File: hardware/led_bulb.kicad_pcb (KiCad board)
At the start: 2 copper layers, 92.4 x 91.4 mm, 170 parts, among them P1 USB_OTG, P10 CONN_01X02, P11 CONN_01X02, P12 CONN_01X02, P13 CONN_01X02, P14 CONN_01X02, P15 CONN_01X02, P16 CONN_01X02, P17 CONN_01X02, P18 CONN_01X02, P19 CONN_01X02, P2 CONN_01X02, P20 CONN_01X02, P21 CONN_01X02, P22 CONN_01X02, P23 CONN_01X02, P24 CONN_01X02, P25 CONN_01X02, P26 CONN_01X02, P27 CONN_01X02, P28 CONN_01X02, P29 CONN_01X02, P3 CONN_01X02, P30 CONN_01X02, P31 CONN_01X02, P32 CONN_01X02, P33 CONN_01X02, P4 CONN_01X02, P5 CONN_01X02, P6 CONN_01X02, P7 CONN_01X02, P8 CONN_01X02, P9 CONN_01X02, Q1 S8050, Q2 S8050, SW1 RST, SW2 FLASH, U1 CP2102-GM, U3 ESP-12E, U4 AP1117D33

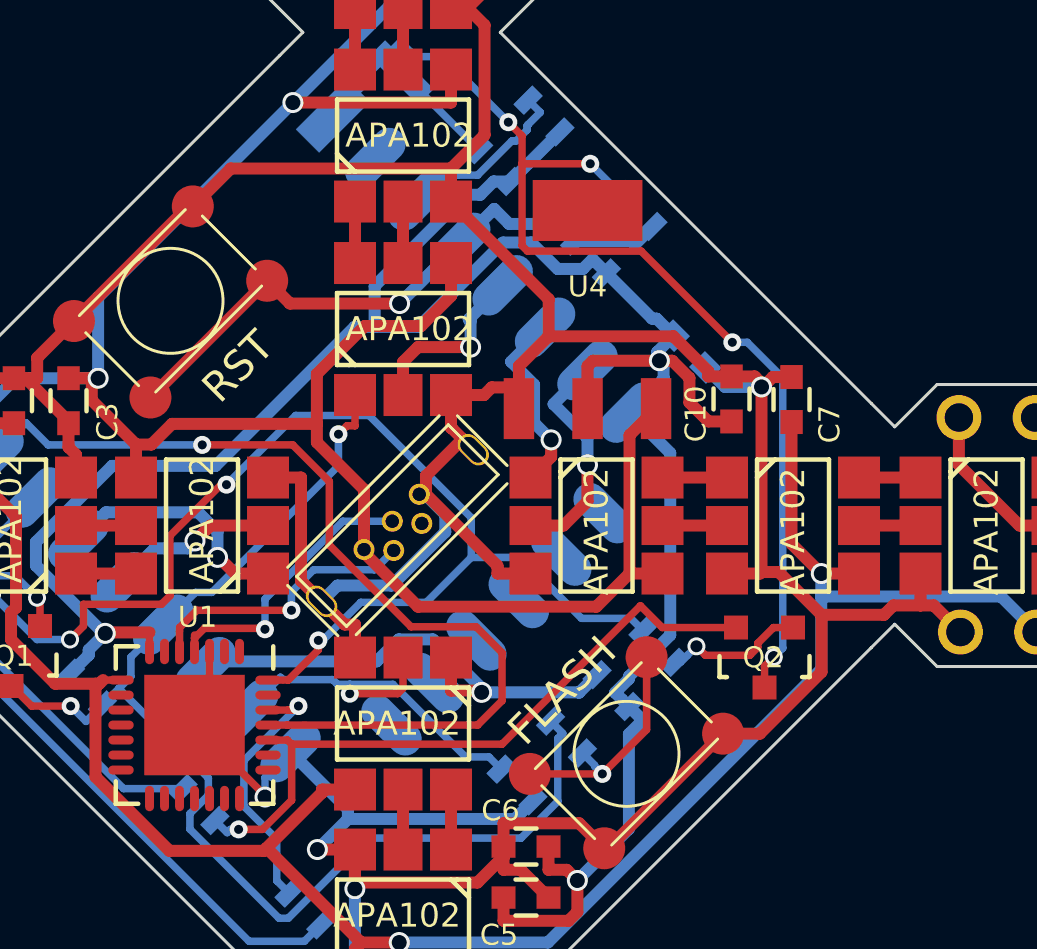
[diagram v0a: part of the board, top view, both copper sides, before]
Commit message: Changed U4/C7/C8/C10 footprint sizes
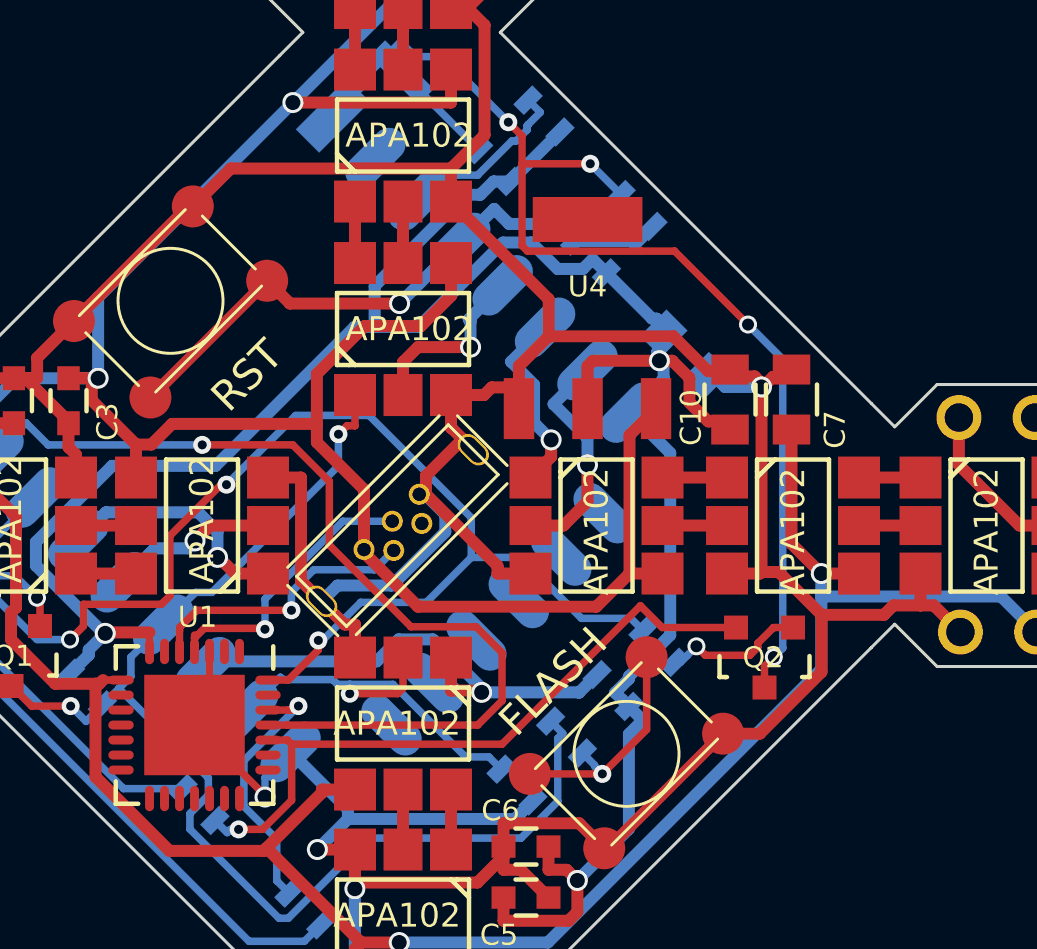
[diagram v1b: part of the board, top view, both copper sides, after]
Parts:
- C10, C7, C8: footprint Capacitors_SMD:C_0603 -> Capacitors_SMD:C_0805
- moved C8 0.18 mm to (115.1, 139.9)
- moved C10 0.05 mm to (116.6, 141.4)
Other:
- board text added: "C10"
- board text added: "C7"
